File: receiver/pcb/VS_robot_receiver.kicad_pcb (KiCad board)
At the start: 2 copper layers, 45 x 21 mm, 6 parts, among them J2 outputs

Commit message: added labels to the receiver outputs
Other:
- board text added: "5"
- board text added: "5V"
- board text added: "6"
- board text added: "7"
- board text added: "8"
- board text added: "GND"

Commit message: pcb cleanup
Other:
- board text added: "1"
- board text added: "13"
- board text added: "Combat Robot Receiver V2"
- board text removed: "Combat Robot Receiver V1"

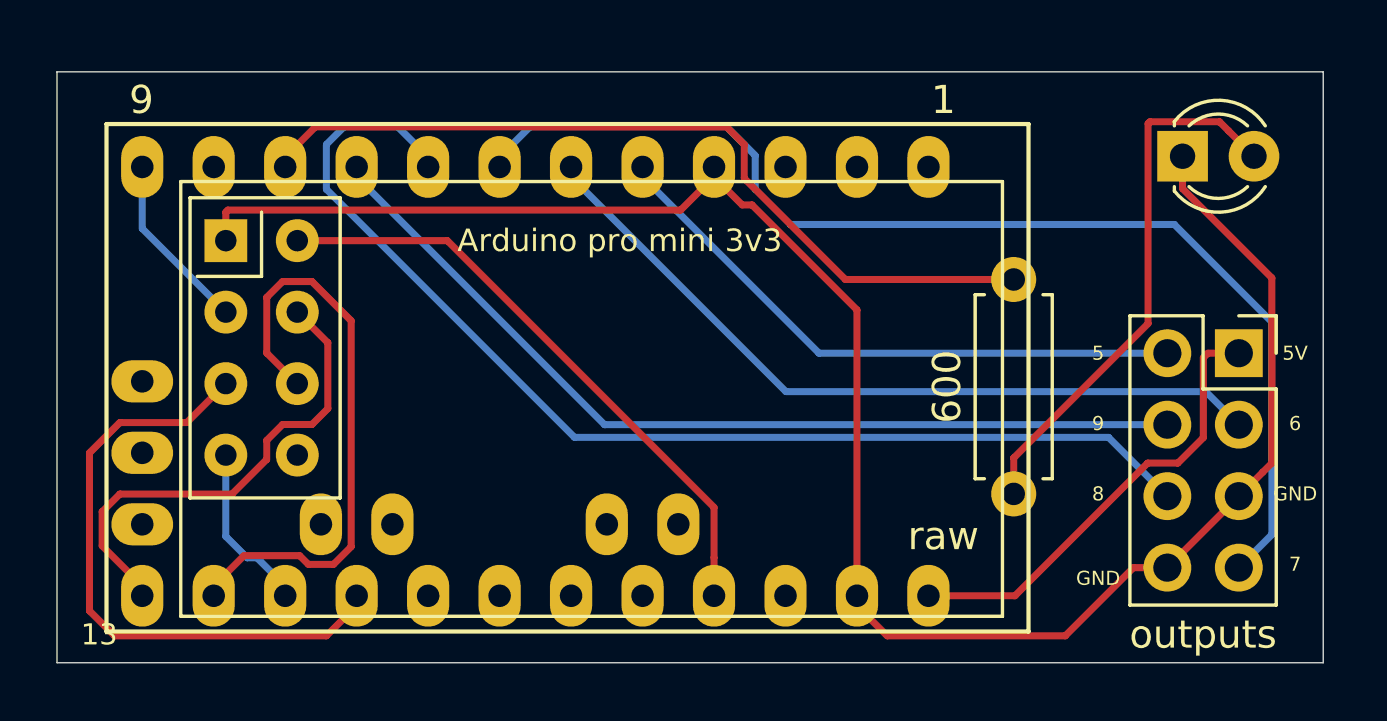
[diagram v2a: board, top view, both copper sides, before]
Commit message: added controllers
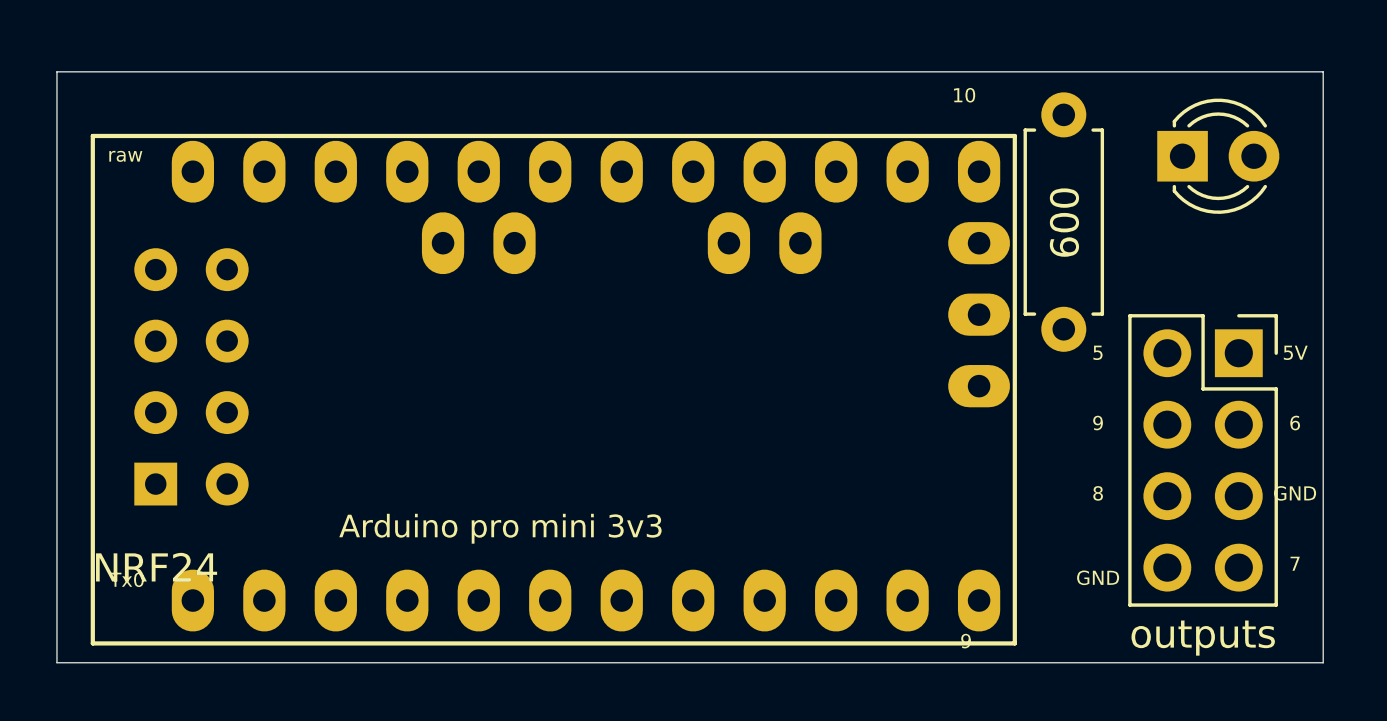
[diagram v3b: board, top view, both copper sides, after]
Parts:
- NRF24: moved to B.Cu
- moved 600 13.6 mm to (165.8, 94.5), turned to 270 degrees
- moved NRF24 9.00 mm to (133.5, 107.7)
- moved Arduino pro mini 3v3 1.81 mm to (148.8, 104.2), turned to 0 degrees
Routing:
- net GND: track 66.7 -> 0.00 mm
- net Net-(J2-Pad7): track 41.0 -> 0.00 mm
- net Net-(J2-Pad6): track 40.7 -> 0.00 mm
- net Net-(J2-Pad4): track 32.8 -> 0.00 mm
- net Net-(R1-Pad2): track 29.6 -> 0.00 mm
- net Net-(J2-Pad3): track 27.7 -> 0.00 mm
- net Net-(U1-Pad16): track 22.1 -> 0.00 mm
- net +3V3: track 21.9 -> 0.00 mm
- net Net-(J2-Pad2): track 21.6 -> 0.00 mm
- net Net-(U1-Pad14): track 21.4 -> 0.00 mm
- net Net-(D1-Pad2): track 19.4 -> 0.00 mm
- net Net-(U1-Pad13): track 17.4 -> 0.00 mm
- net +5V: track 16.3 -> 0.00 mm
- net Net-(U1-Pad12): track 6.39 -> 0.00 mm
- net Net-(U1-Pad15): track 6.08 -> 0.00 mm
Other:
- board text added: "10"
- board text added: "Tx0"
- board text removed: "1"
- board text removed: "13"

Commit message: rewired the output pins for betting intuition and labeling
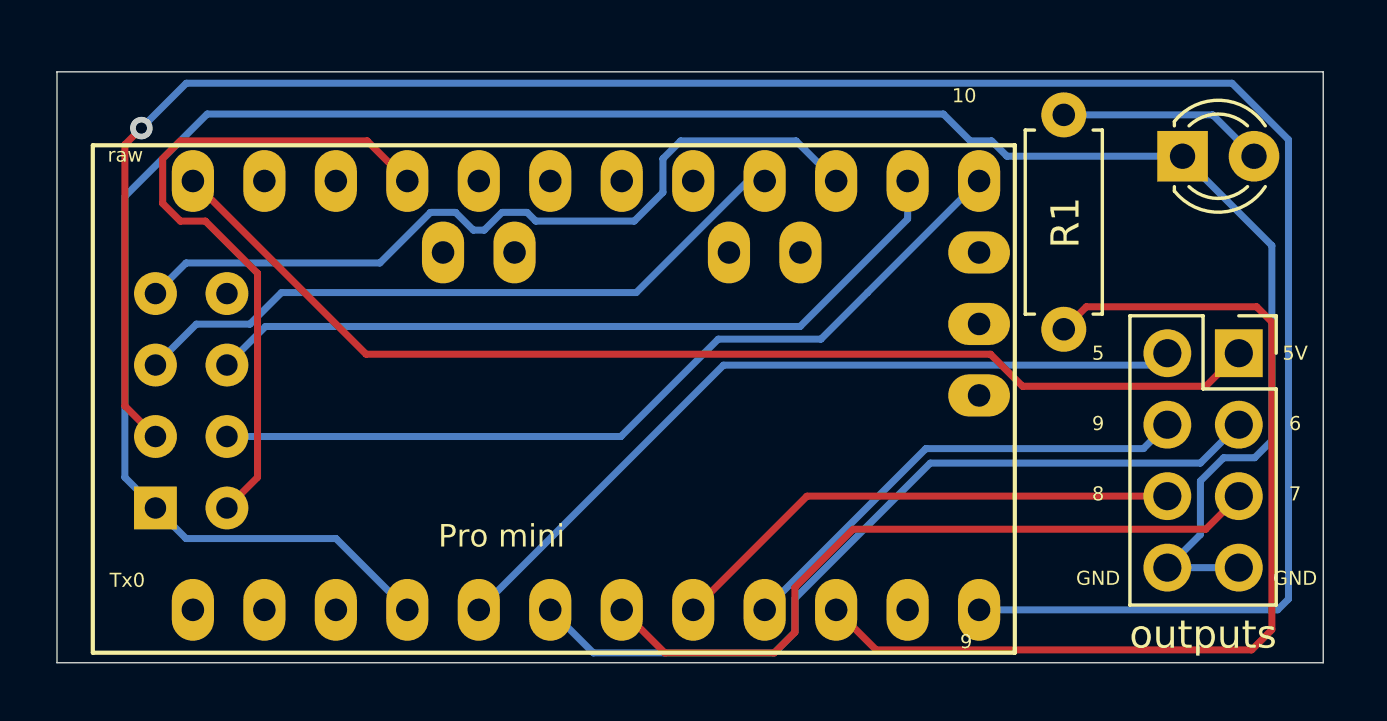
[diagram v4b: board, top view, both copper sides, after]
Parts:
- removed G***: LOGO, vslogo:vslogo
- Pro mini: renamed from Arduino pro mini 3v3
- moved NRF24L01 0.85 mm to (133.5, 108.5)
- moved Pro mini 0.33 mm to (148.8, 104.5)
- renumbered NRF24 to NRF24L01, 600 to R1
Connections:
- J2 pad 5: GND -> Net-(J2-Pad5)
- J2 pad 7: Net-(J2-Pad7) -> GND
- Pro mini pad 23: GND -> Net-(U1-Pad23)
- Pro mini pad 7: Net-(J2-Pad7) -> Net-(J2-Pad5)
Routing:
- net GND: track 0.00 -> 82.1 mm
- net Net-(U1-Pad12): track 0.00 -> 81.4 mm, vias 0 -> 1
- net +5V: track 0.00 -> 40.7 mm
- net Net-(R1-Pad2): track 0.00 -> 35.3 mm
- net Net-(U1-Pad13): track 0.00 -> 30.5 mm
- net Net-(J2-Pad3): track 0.00 -> 29.2 mm
- net Net-(U1-Pad15): track 0.00 -> 28.5 mm
- net Net-(J2-Pad2): track 0.00 -> 28.2 mm
- net Net-(U1-Pad14): track 0.00 -> 27.7 mm
- net Net-(J2-Pad5): track 0.00 -> 25.8 mm
- net Net-(U1-Pad16): track 0.00 -> 24.4 mm
- net +3V3: track 0.00 -> 24.3 mm
- net Net-(J2-Pad6): track 0.00 -> 18.5 mm
- net Net-(J2-Pad4): track 0.00 -> 17.0 mm
- net Net-(D1-Pad2): track 0.00 -> 7.37 mm
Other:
- board text added: "Combat Robot Receiver V1.1"
- board text removed: "Combat Robot Receiver V2"

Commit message: added logo on receiver board
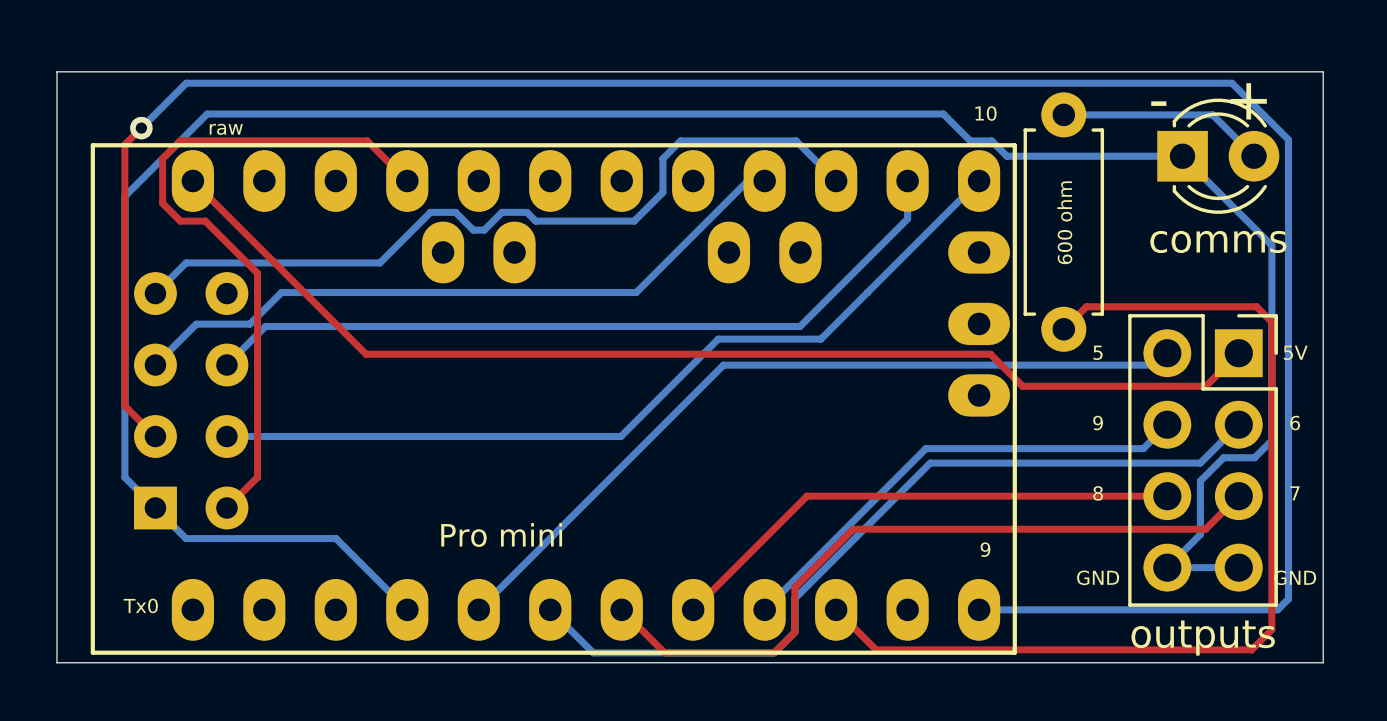
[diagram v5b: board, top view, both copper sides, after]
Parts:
- added G***: LOGO, vslogo:vslogo, B.Cu at (150.0, 105.5)
- 600 ohm: renamed from R1

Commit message: change 5v label to Vin
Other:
- board text added: "Vin"
- board text removed: "5V"

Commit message: changed receiver pin labeling
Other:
- board text added: "1A"
- board text added: "1B"
- board text added: "2A"
- board text added: "2B"
- board text added: "W"
- board text removed: "5"
- board text removed: "6"
- board text removed: "7"
- board text removed: "8"

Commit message: updated version number
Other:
- board text added: "Combat Robot Receiver V1.2"
- board text removed: "Combat Robot Receiver V1.1"
